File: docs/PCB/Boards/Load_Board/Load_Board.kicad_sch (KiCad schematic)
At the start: 7 parts, among them J1 Conn_02x04_Odd_Even, J2 Conn_02x04_Odd_Even, U1 NE555P

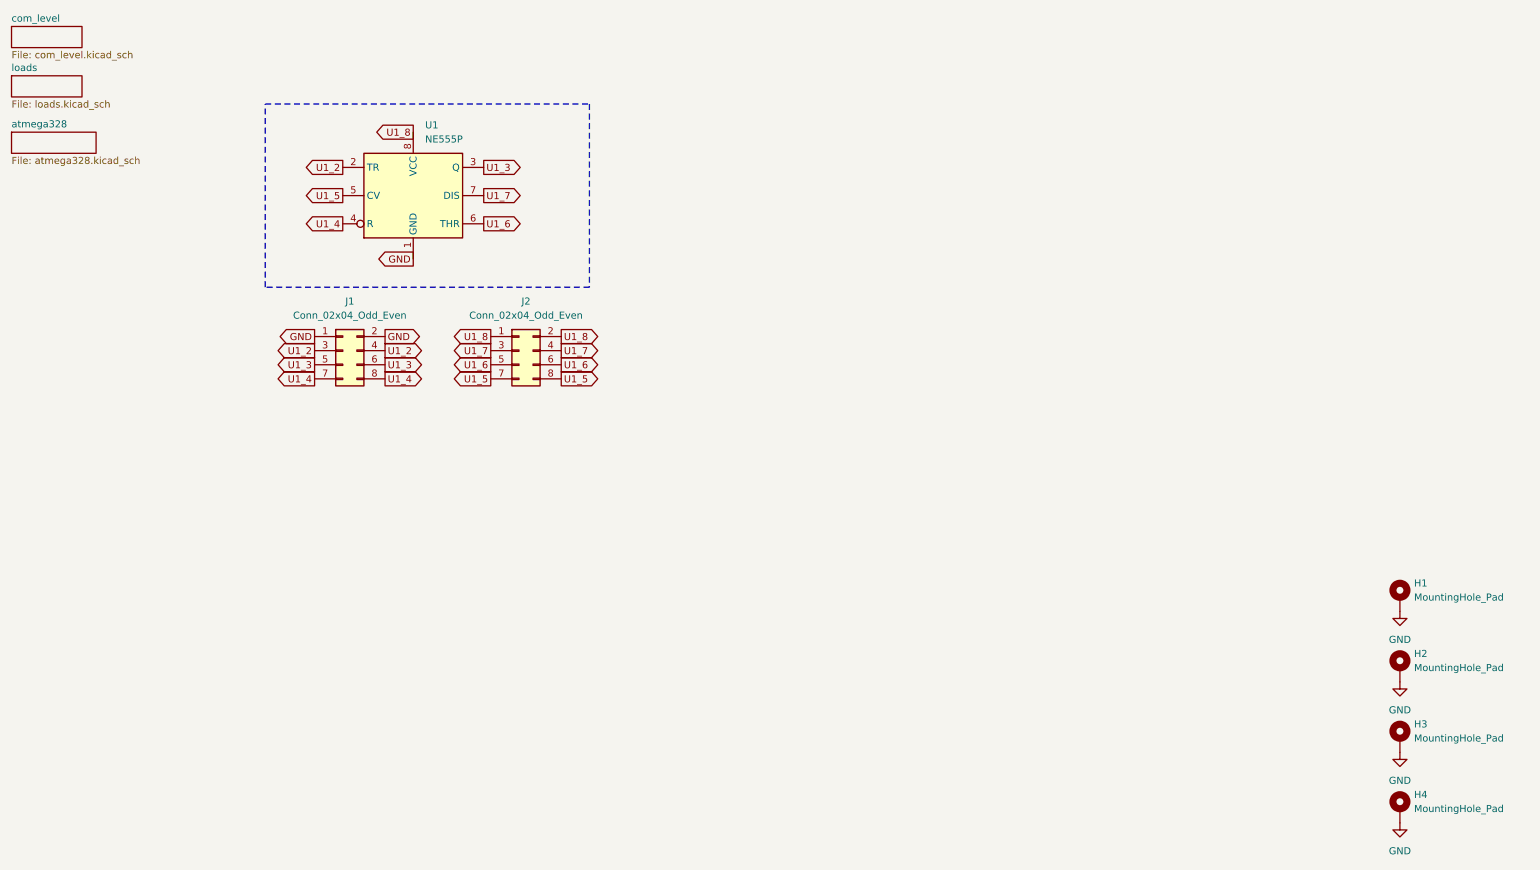
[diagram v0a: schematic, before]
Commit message: Load board and ATMega Board added
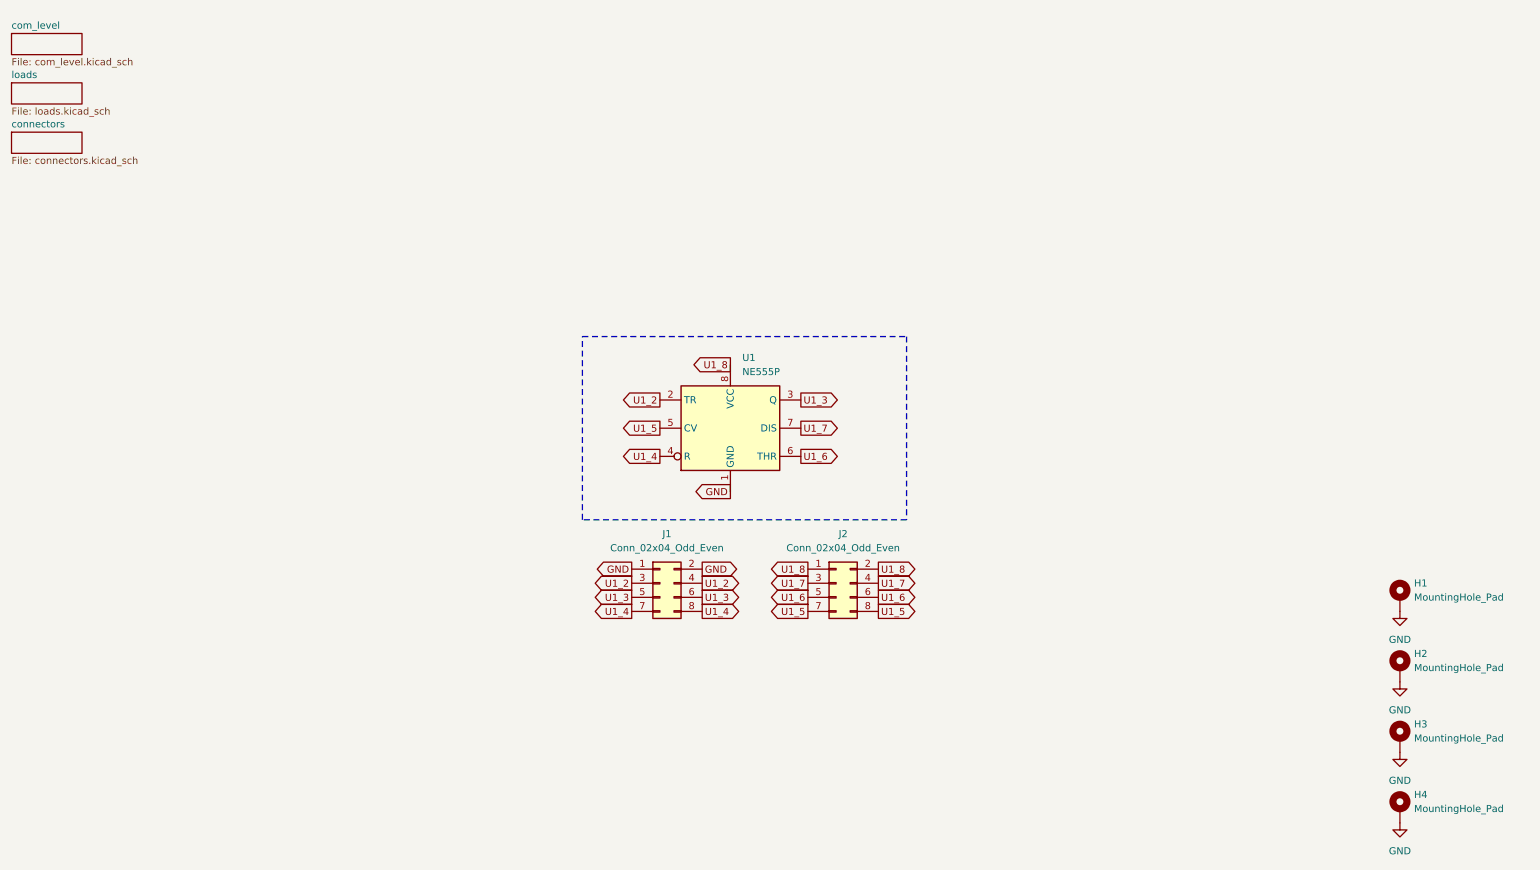
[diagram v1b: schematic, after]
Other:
- removed sheet atmega328
- added sheet connectors (connectors.kicad_sch)
- moved on the sheet: J1, J2, U1
